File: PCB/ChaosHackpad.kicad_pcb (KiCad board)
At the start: 2 copper layers, 81 x 61.7 mm, 22 parts, among them SW1 RotaryEncoder_Switch, SW2 SW_Push_45deg, SW3 SW_Push_45deg, SW4 SW_Push_45deg, SW5 SW_Push_45deg, SW6 SW_Push_45deg, SW7 SW_Push_45deg, SW8 SW_Push_45deg, U1 XIAO-RP2040-DIP

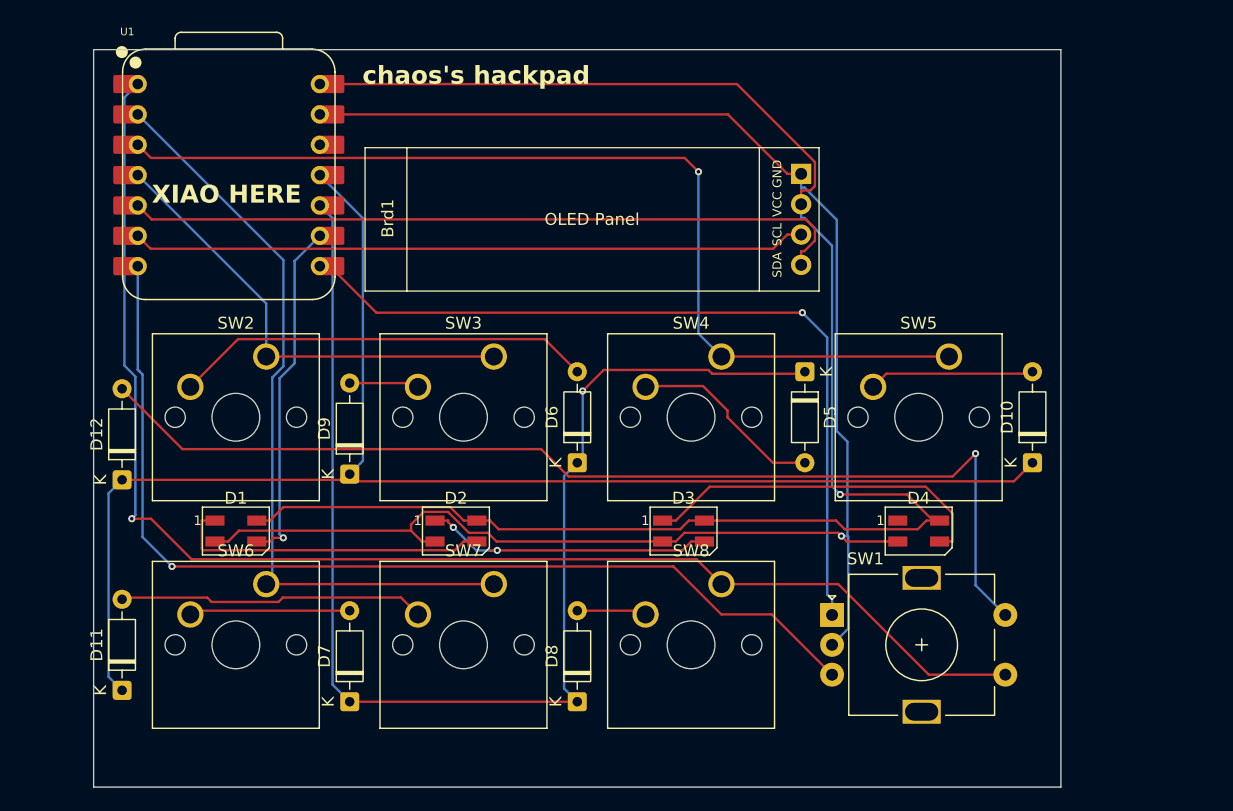
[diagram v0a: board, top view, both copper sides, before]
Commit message: rerouted and redesigned PCB, fixed broken footprints/symbols
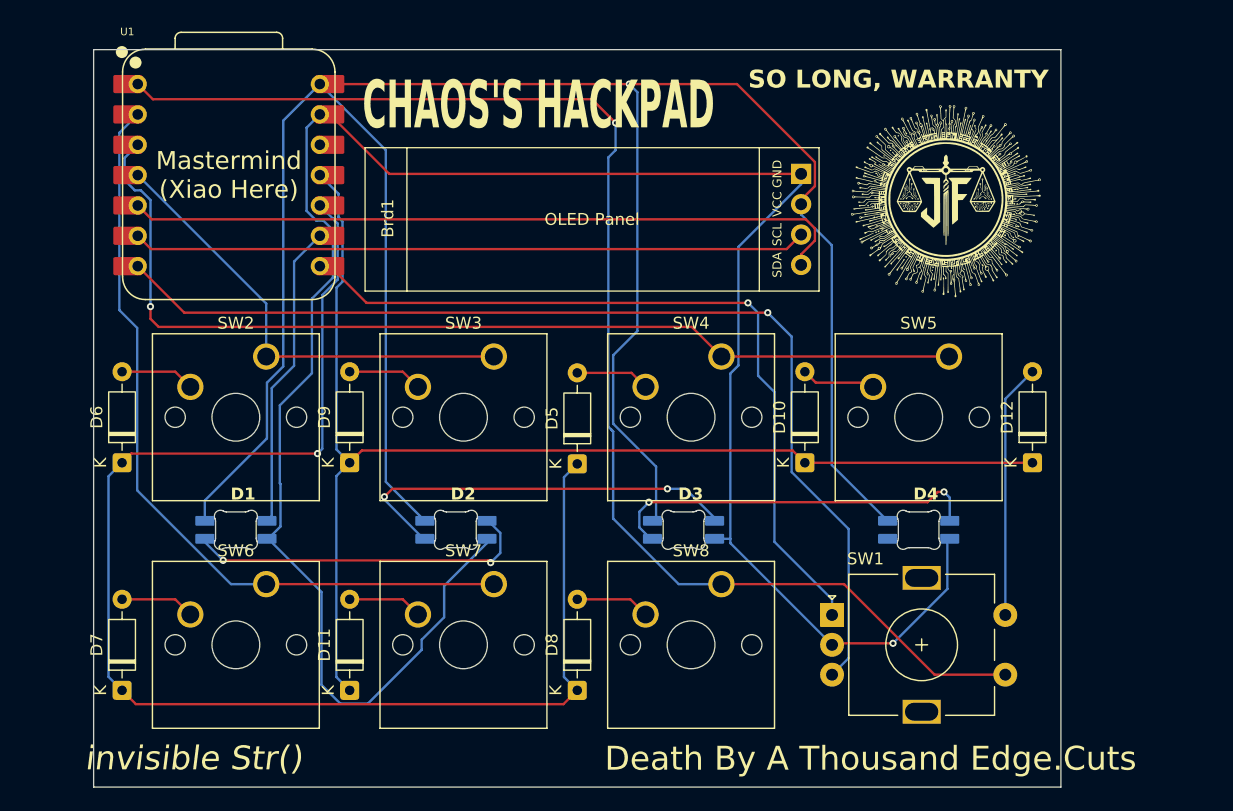
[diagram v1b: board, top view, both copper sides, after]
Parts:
- added G***: LOGO, LOGO, B.Cu at (193.9, 87.3)
- added G1: LOGO, LOGO, F.Cu at (254.8, 86.8)
- D1, D2, D3, D4: footprint LED_SMD:LED_SK6812MINI_PLCC4_3.5x3.5mm_P1.75mm -> SK6812MINI-E:SK6812MINI-E_fixed
- moved D12 76.2 mm to (261.9, 108.6)
- moved D6 38.1 mm to (185.7, 108.6)
- moved D5 20.6 mm to (223.8, 108.7), turned to 90 degrees
- moved D7 19.1 mm to (185.7, 127.6)
- moved D10 19.1 mm to (242.9, 108.6)
- moved D11 19.0 mm to (204.8, 127.6)
- moved D8 0.95 mm to (223.8, 127.6)
- moved D9 0.95 mm to (204.8, 108.6)
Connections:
- D1 pad 1: Net-(D1-DOUT) -> +5V
- D1 pad 2: GND -> Net-(D1-VSS)
- D1 pad 3: NEOIN -> GND
- D1 pad 4: +5V -> NEOIN
- D2 pad 1: Net-(D2-DOUT) -> +5V
- D2 pad 2: GND -> Net-(D2-VSS)
- D2 pad 3: Net-(D1-DOUT) -> GND
- D2 pad 4: +5V -> Net-(D1-VSS)
- D3 pad 1: Net-(D3-DOUT) -> +5V
- D3 pad 2: GND -> Net-(D3-VSS)
- D3 pad 3: Net-(D2-DOUT) -> GND
- D3 pad 4: +5V -> Net-(D2-VSS)
- D4 pad 1: unconnected-(D4-DOUT-Pad1) -> +5V
- D4 pad 2: GND -> unconnected-(D4-DOUT-Pad2)
- D4 pad 3: Net-(D3-DOUT) -> GND
- D4 pad 4: +5V -> Net-(D3-VSS)
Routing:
- net ROTENCS2: track 89.8 -> 21.3 mm, vias 1 -> 0
- net +5V: track 142.4 -> 197.7 mm
- net Net-(D2-VSS): track 0.00 -> 34.2 mm, vias 0 -> 2
- net GND: track 147.1 -> 181.1 mm
- net Net-(D3-VSS): track 0.00 -> 31.6 mm, vias 0 -> 2
- net Net-(D1-VSS): track 0.00 -> 30.3 mm, vias 0 -> 2
- net Net-(D3-DOUT): track 29.8 -> 0.00 mm
- net Net-(D6-A): track 35.2 -> 6.24 mm
- net Net-(D2-DOUT): track 27.2 -> 0.00 mm, vias 2 -> 0
- net Net-(D1-DOUT): track 26.8 -> 0.00 mm
- net Net-(D11-A): track 25.7 -> 6.24 mm
- net ROW1: track 123.7 -> 104.5 mm
- net Net-(D5-A): track 16.4 -> 6.20 mm
- net ROW0: track 109.1 -> 118.8 mm
- net Net-(D10-A): track 13.9 -> 6.24 mm
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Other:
- board text added: "CHAOS'S HACKPAD"
- board text added: "Death By A Thousand Edge.Cuts"
- board text added: "Mastermind (Xiao Here)"
- board text added: "SO LONG, WARRANTY"
- board text added: "invisible Str()"
- board text removed: "XIAO HERE"
- board text removed: "chaos's hackpad"

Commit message: changed layout
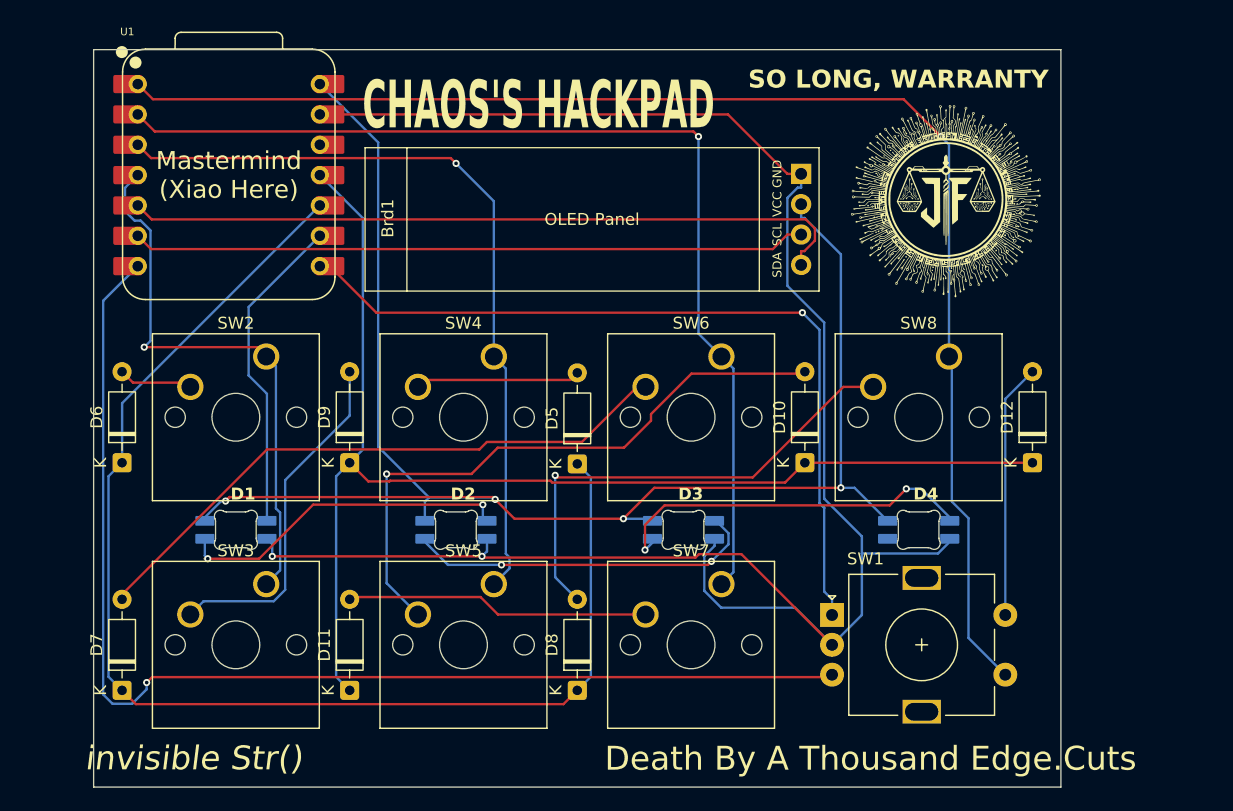
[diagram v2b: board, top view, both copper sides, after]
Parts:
- moved SW5 42.6 mm to (216.9, 118.7)
- moved SW6 42.6 mm to (235.9, 99.7)
- moved SW3 26.9 mm to (197.8, 118.7)
- moved SW8 26.9 mm to (255.0, 99.7)
- moved SW4 19.1 mm to (216.9, 99.7)
- moved SW7 19.1 mm to (235.9, 118.7)
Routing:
- net +5V: track 197.7 -> 137.7 mm, vias 1 -> 4
- net Net-(D10-A): track 6.24 -> 51.7 mm, vias 0 -> 1
- net Net-(D7-A): track 6.24 -> 51.4 mm
- net Net-(D8-A): track 6.24 -> 41.0 mm, vias 0 -> 1
- net Net-(D9-A): track 6.24 -> 29.3 mm
- net COL2: track 66.7 -> 87.6 mm, vias 0 -> 1
- net COL1: track 85.2 -> 65.7 mm
- net Net-(D11-A): track 6.24 -> 25.4 mm
- net GND: track 181.1 -> 164.8 mm, vias 1 -> 2
- net Net-(U1-GPIO0/TX): track 88.9 -> 100.5 mm
- net ROW0: track 118.8 -> 108.2 mm, vias 1 -> 0
- net COL0: track 39.5 -> 47.6 mm, vias 0 -> 1
- net Net-(D5-A): track 6.20 -> 13.8 mm
- net Net-(D2-VSS): track 34.2 -> 29.7 mm
- net COL3: track 114.2 -> 117.2 mm
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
